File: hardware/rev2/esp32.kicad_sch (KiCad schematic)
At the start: 29 parts, among them J6 SMA, SW1 SW_Push, U1 ESP32-S3, Y1 Crystal_GND24

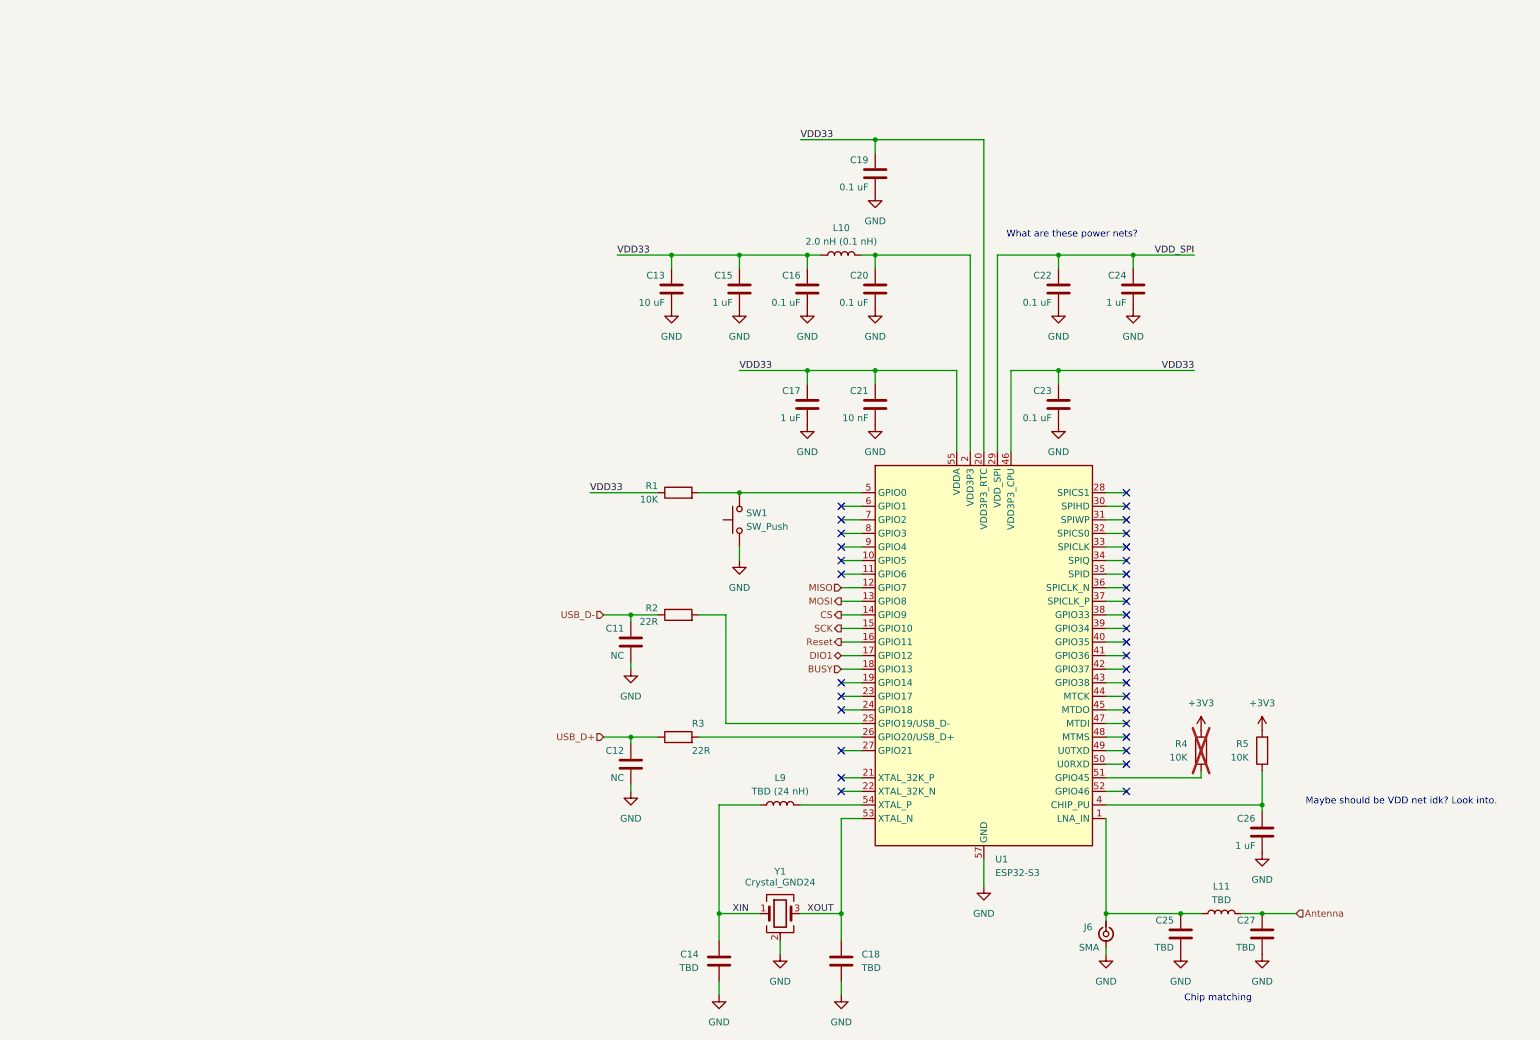
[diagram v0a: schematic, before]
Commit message: ESP32 approaching final schematic. tidied up a lot and changed GPIO pins.
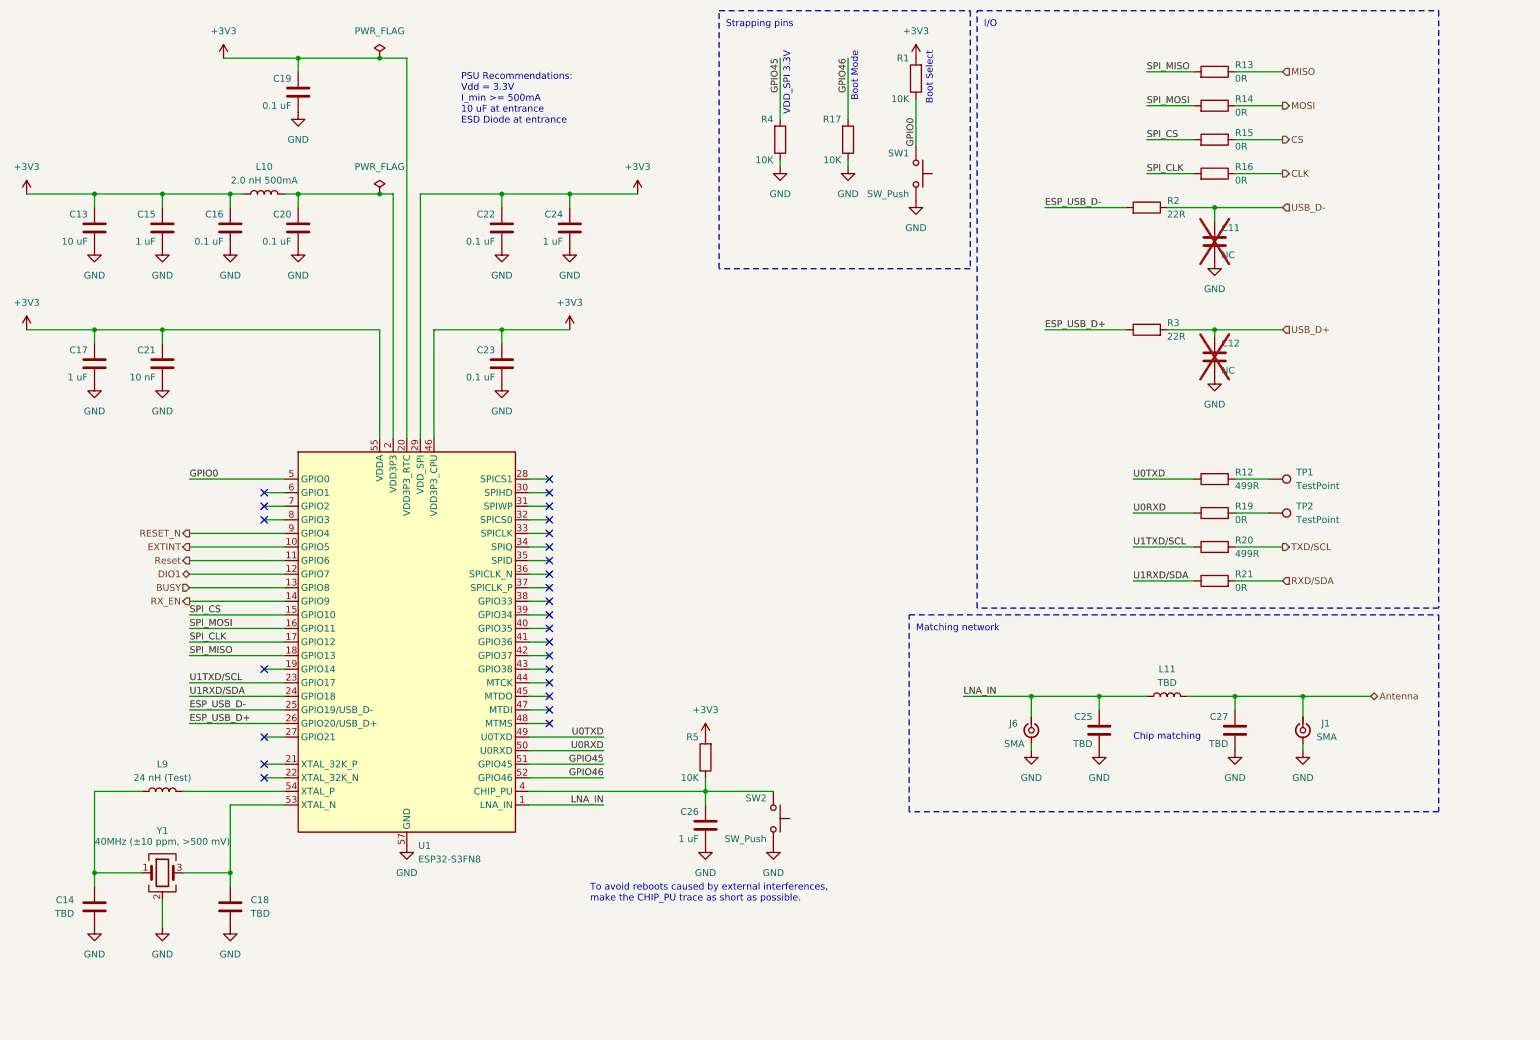
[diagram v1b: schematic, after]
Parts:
- added J1: SMA, symbol Connector:Conn_Coaxial_Small
- added R12, R20: 499R, Inductor_SMD:L_0603_1608Metric_Pad1.05x0.95mm_HandSolder, symbol Device:R
- added R13, R14, R15, R16: 0R, symbol Device:R
- added R17: 10K, Inductor_SMD:L_0603_1608Metric_Pad1.05x0.95mm_HandSolder, symbol Device:R
- added R19, R21: 0R, Inductor_SMD:L_0603_1608Metric_Pad1.05x0.95mm_HandSolder, symbol Device:R
- added SW2: SW_Push, Button_Switch_SMD:SW_Push_1P1T_NO_CK_KSC7xxJ, symbol Switch:SW_Push
- added TP1, TP2: TestPoint, symbol Connector:TestPoint
- C11, C12: now not fitted
- L10: value 2.0 nH (0.1 nH) -> 2.0 nH 500mA
- L9: value TBD (24 nH) -> 24 nH (Test)
- R4: now fitted
- U1: value ESP32-S3 -> ESP32-S3FN8
- Y1: value Crystal_GND24 -> 40MHz (±10 ppm, >500 mV)
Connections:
- net VDD_SPI is gone; now on net +3V3: C22.1, C24.1, U1.29 (VDD_SPI)
- net +3V3: now also C13.1, C15.1, C16.1, C17.1, C19.1, C21.1, C23.1, L10.1, R1.2, U1.20 (VDD3P3_RTC), U1.46 (VDD3P3_CPU), U1.55 (VDDA), U1.56 (VDDA); no longer R4.1
- net Antenna: now also J1.1 (In)
- net BUSY: now also U1.13 (GPIO8); no longer U1.18 (GPIO13)
- net CS: now also R15.1; no longer U1.14 (GPIO9)
- net DIO1: now also U1.12 (GPIO7); no longer U1.17 (GPIO12)
- net GND: now also R4.1, J1.2 (Ext), R17.1, SW2.1
- net MISO: now also R13.1; no longer U1.12 (GPIO7)
- net MOSI: now also R14.1; no longer U1.13 (GPIO8)
- net Reset: now also U1.11 (GPIO6); no longer U1.16 (GPIO11)
- net USB_D+: now also R3.2; no longer R3.1
- net at C26.1, R5.1, U1.4 (CHIP_PU): now also SW2.2
- net GPIO45: now reaches R4.2, U1.51 (GPIO45)
- net LNA_IN: now reaches C25.1, J6.1 (In), L11.2, U1.1 (LNA_IN)
- net ESP_USB_D+: now reaches U1.26 (GPIO20/USB_D+)
- net ESP_USB_D+: now also R3.1; no longer R3.2
- net GPIO0: now reaches SW1.2, U1.5 (GPIO0)
- net GPIO0: now also R1.1; no longer R1.2
- net EXTINT: now reaches U1.10 (GPIO5)
- net U1TXD/SCL: now reaches U1.23 (GPIO17)
- net U1TXD/SCL: now also R20.1
- net U1RXD/SDA: now reaches U1.24 (GPIO18)
- net U1RXD/SDA: now also R21.1
- net ESP_USB_D-: now reaches R2.2, U1.25 (GPIO19/USB_D-)
- net U0TXD: now reaches U1.49 (U0TXD)
- net U0TXD: now also R12.1
- net U0RXD: now reaches U1.50 (U0RXD)
- net U0RXD: now also R19.1
- net GPIO46: now reaches U1.52 (GPIO46)
- net GPIO46: now also R17.2
- net RESET_N: now reaches U1.9 (GPIO4)
- net SCK renamed SPI_CS
- net SPI_CS: now also R15.2
- removed net VDD33: C13.1, C15.1, C16.1, C17.1, C19.1, C21.1, C23.1, L10.1, R1.1, U1.20 (VDD3P3_RTC), U1.46 (VDD3P3_CPU), U1.55 (VDDA), U1.56 (VDDA)
- net XIN: no longer names the net of C14.1, L9.1, Y1.1
- net XOUT: no longer names the net of C18.1, U1.53 (XTAL_N), Y1.3
- new net: R19.2, TP2.1
- new net: R12.2, TP1.1
- new net CLK: R16.1
- new net RXD/SDA: R21.2
- new net RX_EN: U1.14 (GPIO9)
- new net SPI_CLK: R16.2, U1.17 (GPIO12)
- new net SPI_MISO: R13.2, U1.18 (GPIO13)
- new net SPI_MOSI: R14.2, U1.16 (GPIO11)
- new net TXD/SCL: R20.2
- no-connect marks 34 -> 26
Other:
- note added: "Boot Mode"
- note added: "Boot Select"
- note added: "I/O"
- note added: "Matching network"
- note added: "PSU Recommendations: Vdd = 3.3V I_min >= 500mA 10 uF at entrance ESD Diode at entrance"
- note added: "Strapping pins"
- note added: "To avoid reboots caused by external interferences, make the CHIP_PU trace as short as possible."
- note added: "VDD_SPI 3.3V"
- note removed: "Maybe should be VDD net idk? Look into."
- note removed: "What are these power nets?"
- company: (none) -> MMCX11
- title: (none) -> ESP32
- moved on the sheet: C13, C14, C15, C16, C17, C18, C19, C20, C21, C22, C23, C24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

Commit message: fixed typo
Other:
- note added: "PSU Recommendations: Vdd = 3.3V I_max >= 500mA 10 uF at entrance ESD Diode at entrance"
- note removed: "PSU Recommendations: Vdd = 3.3V I_min >= 500mA 10 uF at entrance ESD Diode at entrance"
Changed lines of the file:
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@@
 		)
 	)
-	(text "PSU Recommendations:\nVdd = 3.3V\nI_min >= 500mA\n10 uF at entrance\nESD Diode at entrance"
+	(text "PSU Recommendations:\nVdd = 3.3V\nI_max >= 500mA\n10 uF at entrance\nESD Diode at entrance"
 		(exclude_from_sim no)
 		(at 100.33 30.48 0)

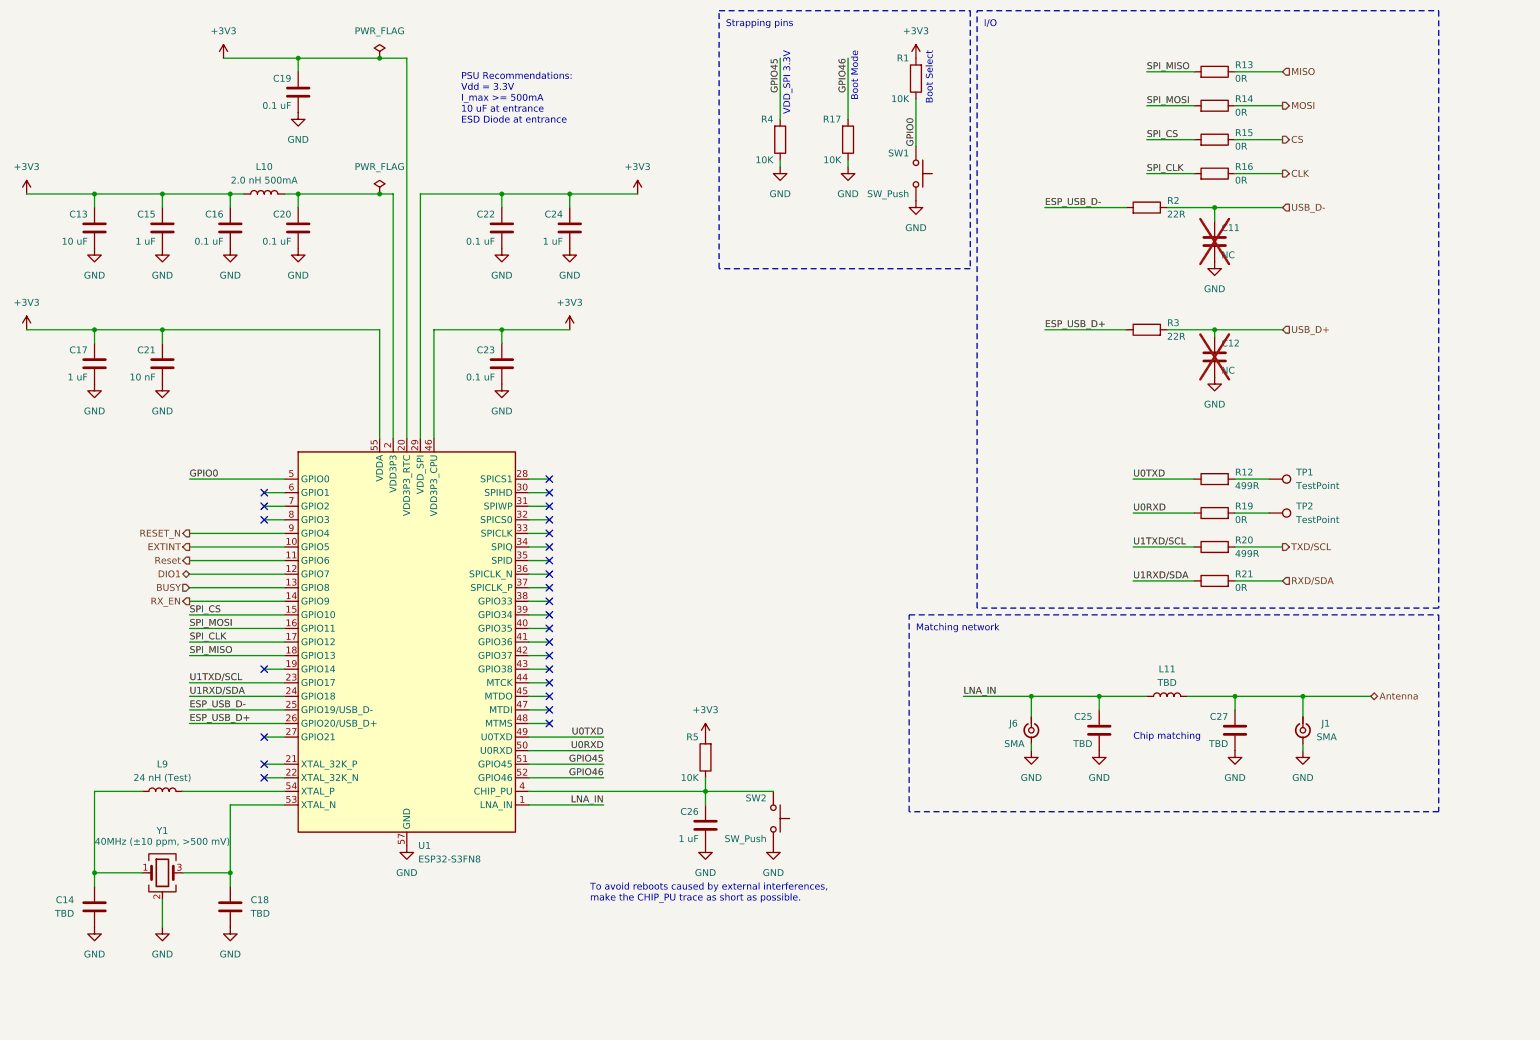
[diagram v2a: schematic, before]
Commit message: redid usb termination and begun adding components from mouser
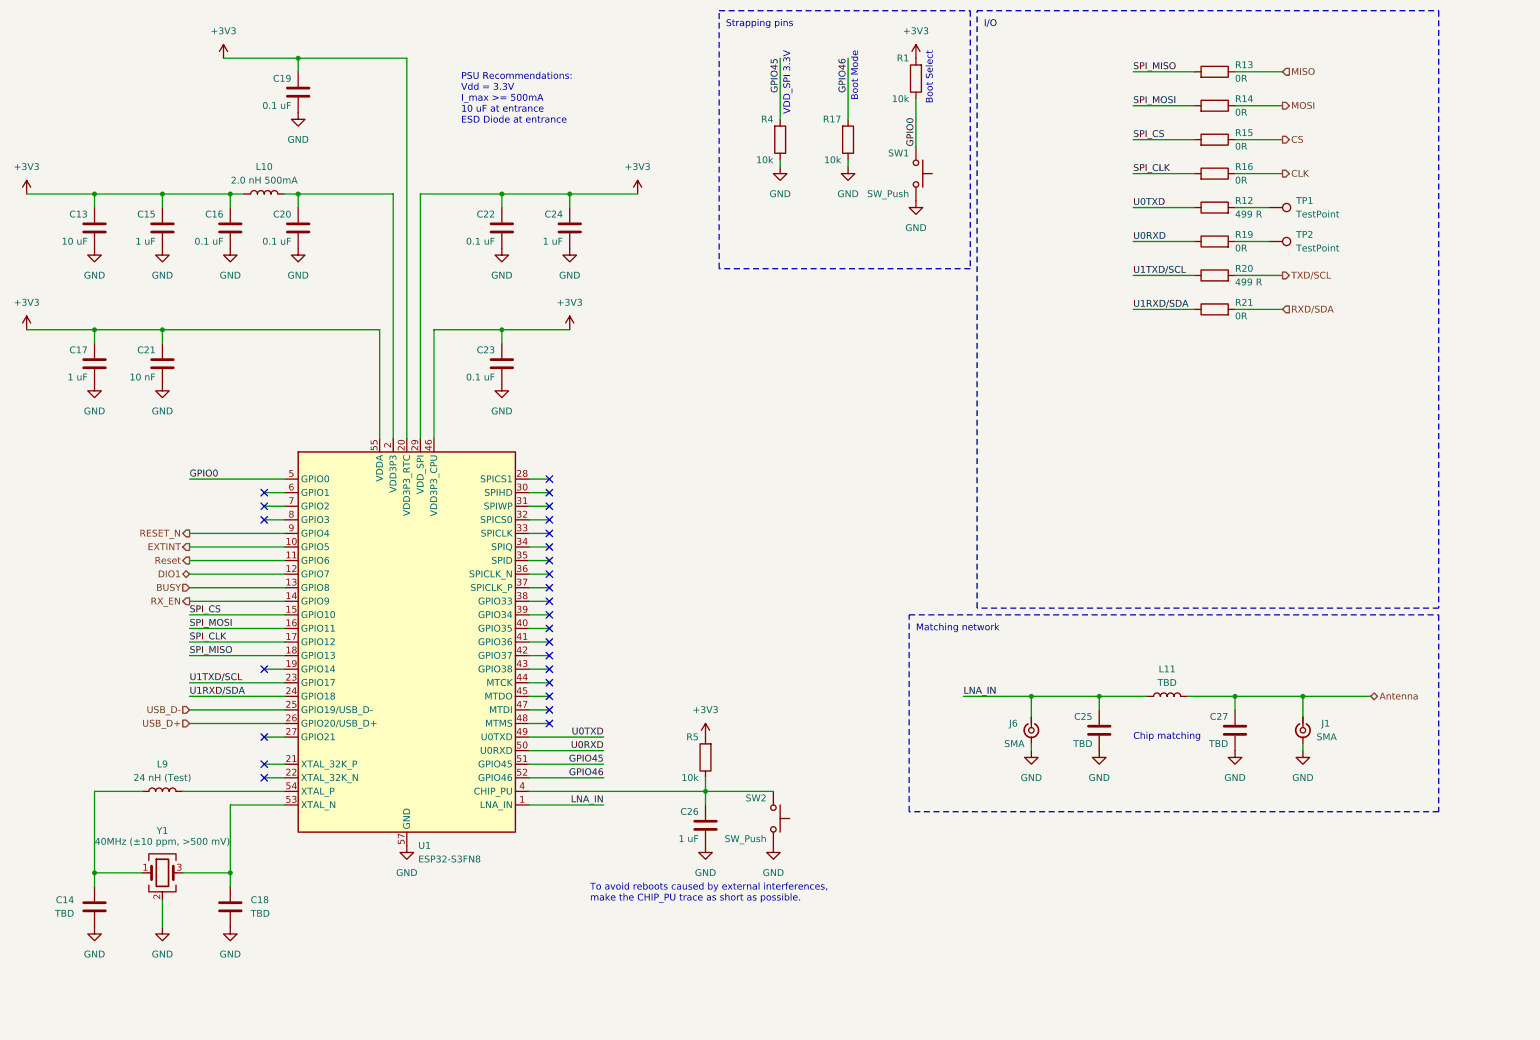
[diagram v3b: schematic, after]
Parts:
- removed C11, C12: NC, Capacitor_SMD:C_0201_0603Metric_Pad0.64x0.40mm_HandSolder, symbol Device:C
- removed R2, R3: 22R, Inductor_SMD:L_0603_1608Metric_Pad1.05x0.95mm_HandSolder, symbol Device:R
- C13: Mouser Part Number (none) -> 81-GRM188D70J106MA3D
- C15, C17, C24, C26: Mouser Part Number (none) -> 81-GRM188C70J105KA1D
- C16, C19, C20, C22, C23: Mouser Part Number (none) -> 81-GCJ188R71E104KA2D
- C21: Mouser Part Number (none) -> 81-GCM188R72A103KA7D
- J1, J6: footprint (none) -> Connector_Coaxial:SMA_Amphenol_132134-16_Vertical; Mouser Part Number (none) -> 640-RFPCSMA28F
- R1, R17, R4, R5: value 10K -> 10k
- R12, R20: value 499R -> 499 R
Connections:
- net ESP_USB_D+ is gone; now on net USB_D+: U1.26 (GPIO20/USB_D+)
- net ESP_USB_D- is gone; now on net USB_D-: U1.25 (GPIO19/USB_D-)
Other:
- moved on the sheet: R12, R19, R20, R21, TP1, TP2

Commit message: set all applicable components for sx1262
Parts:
- C15, C17, C24, C26: Mouser Part Number 81-GRM188C70J105KA1D -> (none)
- R13, R14, R15, R16: footprint (none) -> Resistor_SMD:R_0603_1608Metric_Pad0.98x0.95mm_HandSolder
- R17, R4: now in the parts list
- R19, R21: footprint Inductor_SMD:L_0603_1608Metric_Pad1.05x0.95mm_HandSolder -> Resistor_SMD:R_0603_1608Metric_Pad0.98x0.95mm_HandSolder; now in the parts list
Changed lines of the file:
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@@
 		(body_style 1)
 		(exclude_from_sim no)
-		(in_bom no)
+		(in_bom yes)
 		(on_board yes)
 		(in_pos_files yes)
@@
 			)
 		)
-		(property "Datasheet" "https://www.mouser.se/datasheet/3/76/3/GRM188C70J105KA01_01A.pdf"
+		(property "Datasheet" ""
 			(at 146.05 166.37 0)
 			(hide yes)
@@
 			)
 		)
-		(property "Mouser Part Number" "81-GRM188C70J105KA1D"
+		(property "Mouser Part Number" ""
 			(at 146.05 166.37 0)
 			(hide yes)
@@
 		(body_style 1)
 		(exclude_from_sim no)
-		(in_bom no)
+		(in_bom yes)
 		(on_board yes)
 		(in_pos_files yes)
@@
 			)
 		)
-		(property "Datasheet" "https://www.mouser.se/datasheet/3/76/3/GRM188C70J105KA01_01A.pdf"
+		(property "Datasheet" ""
 			(at 120.65 54.61 0)
 			(hide yes)
@@
 			)
 		)
-		(property "Mouser Part Number" "81-GRM188C70J105KA1D"
+		(property "Mouser Part Number" ""
 			(at 120.65 54.61 0)
 			(hide yes)
@@
 		(body_style 1)
 		(exclude_from_sim no)
-		(in_bom no)
+		(in_bom yes)
 		(on_board yes)
 		(in_pos_files yes)
@@
 			)
 		)
-		(property "Footprint" "Inductor_SMD:L_0603_1608Metric_Pad1.05x0.95mm_HandSolder"
+		(property "Footprint" "Resistor_SMD:R_0603_1608Metric_Pad0.98x0.95mm_HandSolder"
 			(at 241.3 71.628 90)
 			(hide yes)
@@
 			)
 		)
-		(property "Datasheet" "https://www.mouser.se/datasheet/3/76/3/GRM188C70J105KA01_01A.pdf"
+		(property "Datasheet" ""
 			(at 31.75 80.01 0)
 			(hide yes)
@@
 			)
 		)
-		(property "Mouser Part Number" "81-GRM188C70J105KA1D"
+		(property "Mouser Part Number" ""
 			(at 31.75 80.01 0)
 			(hide yes)
@@
 			)
 		)
-		(property "Datasheet" "https://www.mouser.se/datasheet/3/76/3/GRM188C70J105KA01_01A.pdf"
+		(property "Datasheet" ""
 			(at 44.45 54.61 0)
 			(hide yes)
@@
 			)
 		)
-		(property "Mouser Part Number" "81-GRM188C70J105KA1D"
+		(property "Mouser Part Number" ""
 			(at 44.45 54.61 0)
 			(hide yes)
@@
 			)
 		)
-		(property "Footprint" ""
+		(property "Footprint" "Resistor_SMD:R_0603_1608Metric_Pad0.98x0.95mm_HandSolder"
 			(at 241.3 46.228 90)
 			(hide yes)
@@
 		(body_style 1)
 		(exclude_from_sim no)
-		(in_bom no)
+		(in_bom yes)
 		(on_board yes)
 		(in_pos_files yes)
@@
 			)
 		)
-		(property "Footprint" "Inductor_SMD:L_0603_1608Metric_Pad1.05x0.95mm_HandSolder"
+		(property "Footprint" "Resistor_SMD:R_0603_1608Metric_Pad0.98x0.95mm_HandSolder"
 			(at 241.3 58.928 90)
 			(hide yes)
@@
 			)
 		)
-		(property "Footprint" ""
+		(property "Footprint" "Resistor_SMD:R_0603_1608Metric_Pad0.98x0.95mm_HandSolder"
 			(at 241.3 27.178 90)
 			(hide yes)
@@
 			)
 		)
-		(property "Footprint" ""
+		(property "Footprint" "Resistor_SMD:R_0603_1608Metric_Pad0.98x0.95mm_HandSolder"
 			(at 241.3 33.528 90)
 			(hide yes)
@@
 			)
 		)
-		(property "Footprint" ""
+		(property "Footprint" "Resistor_SMD:R_0603_1608Metric_Pad0.98x0.95mm_HandSolder"
 			(at 241.3 39.878 90)
 			(hide yes)
